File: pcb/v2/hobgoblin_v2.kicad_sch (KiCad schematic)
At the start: 47 parts, among them J1 5V, J2 RC2014EXT1, J3 RC2014EXT2, SW1 RESET, SW2 ROMBNK, SW3 USBUART, U1 74LS32, U10 MC68B50, U2 74LS14, U3 Z80CPU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

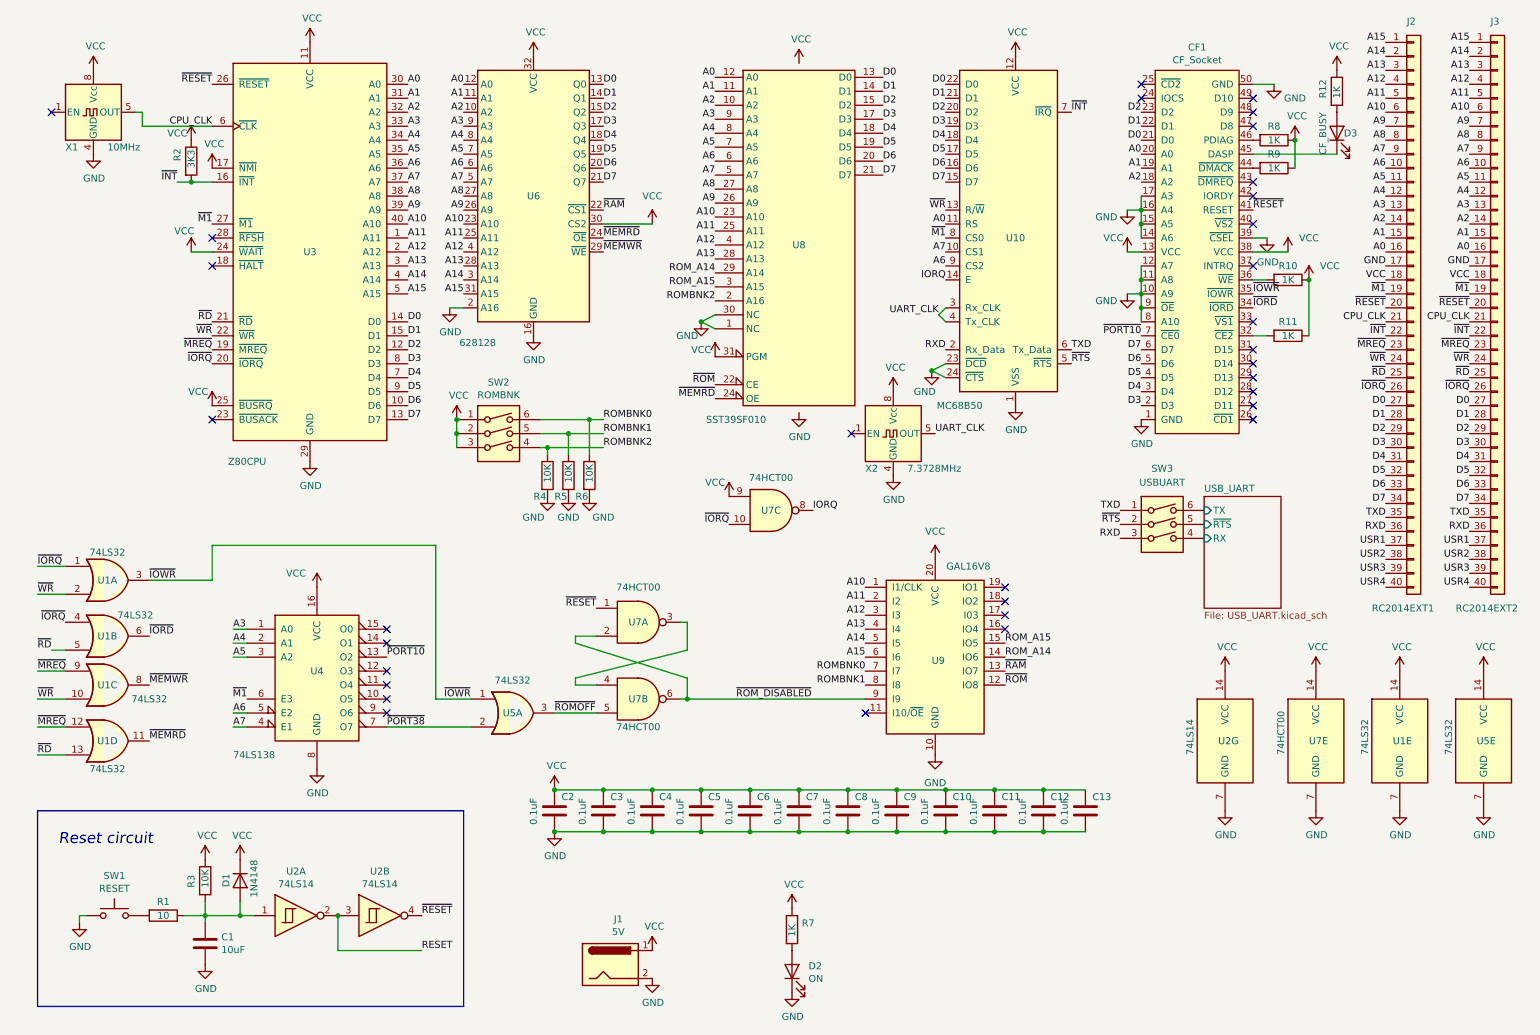
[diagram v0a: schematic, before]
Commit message: Start using GALs in V2
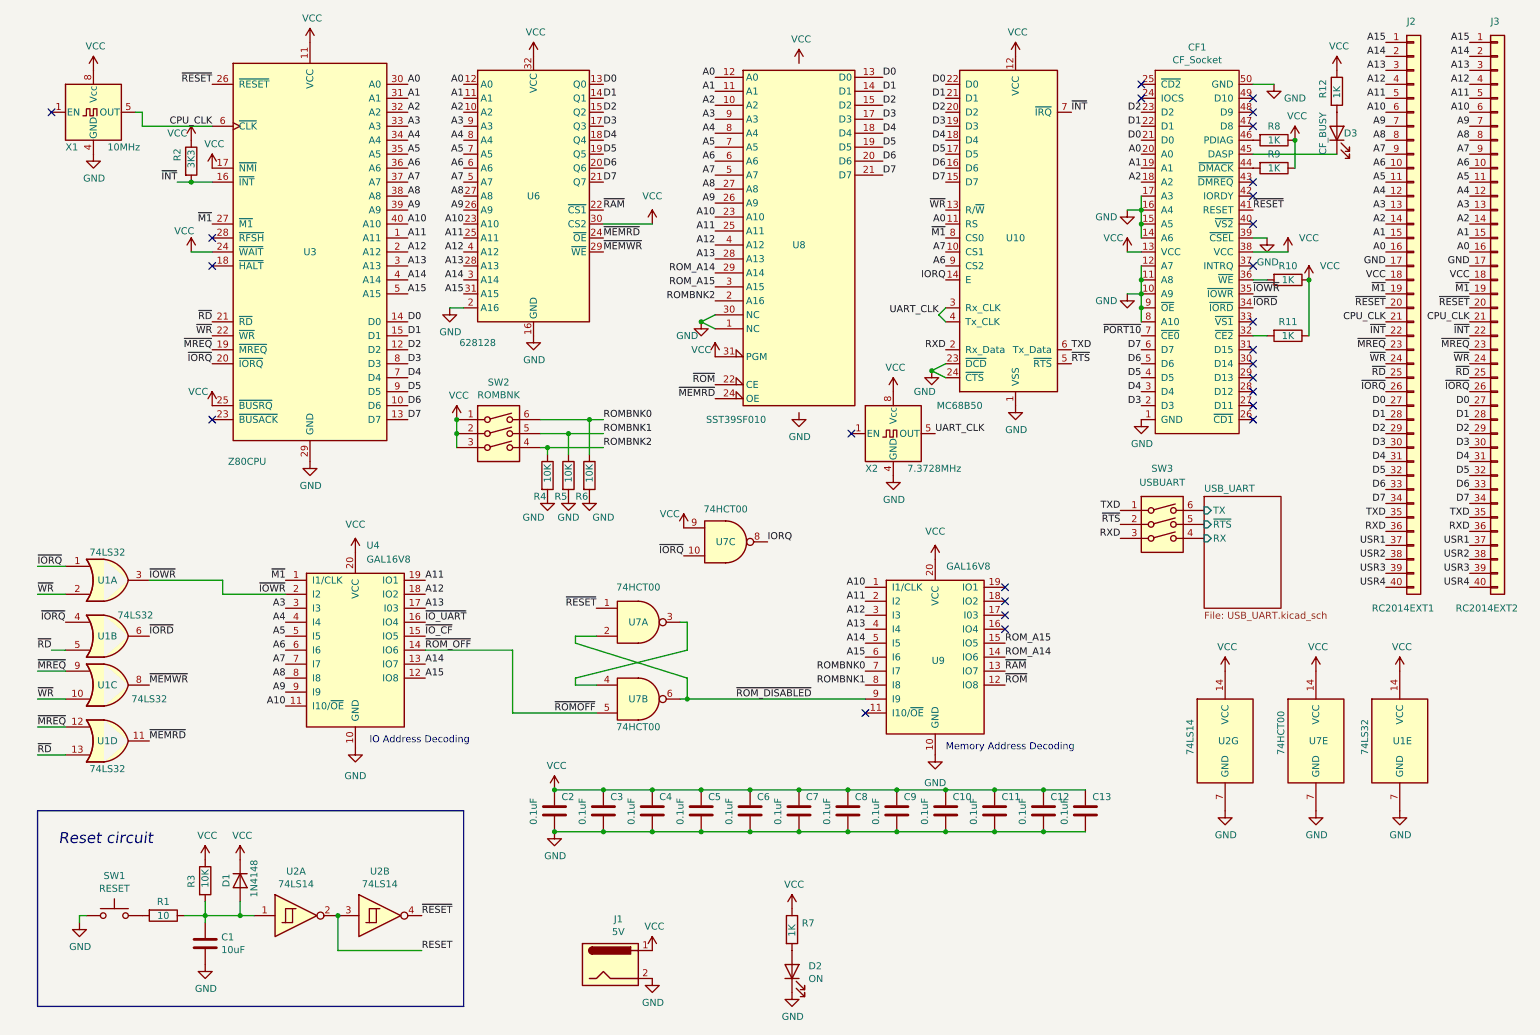
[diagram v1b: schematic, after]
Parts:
- removed U4: 74LS138, Package_DIP:DIP-16_W7.62mm_LongPads, symbol 74xx:74LS138
- removed U5: 74LS32, Package_DIP:DIP-14_W7.62mm_LongPads, symbol 74xx:74LS32
- added U4: GAL16V8, Package_DIP:DIP-20_W7.62mm_Socket_LongPads, symbol Logic_Programmable:GAL16V8
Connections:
- net A10: now also U4.11 (I10/~{OE})
- net A11: now also U4.19 (IO1)
- net A12: now also U4.18 (IO2)
- net A13: now also U4.17 (I03)
- net A14: now also U4.13 (IO7)
- net A15: now also U4.12 (IO8)
- net A3: now also U4.3 (I3)
- net A4: now also U4.4 (I4)
- net A5: now also U4.5 (I5)
- net A6: now also U4.6 (I6)
- net A7: now also U4.7 (I7)
- net A8: now also U4.8 (I8)
- net A9: now also U4.9 (I9)
- net GND: now also U4.10 (GND)
- net VCC: now also U4.20 (VCC)
- net ~{IOWR}: now also U4.2 (I2)
- net ~{M1}: now also U4.1 (I1/CLK)
- net ~{ROMOFF}: now also U4.14 (IO6)
- new net ~{IO_CF}: U4.15 (IO5)
- new net ~{IO_UART}: U4.16 (IO4)
- no-connect marks 32 -> 26
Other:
- note added: "IO Address Decoding"
- note added: "Memory Address Decoding"
- moved on the sheet: U7C

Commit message: Draft component placement
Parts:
- U4: value GAL16V8 -> GAL16V8/IO
- U9: value GAL16V8 -> GAL16V8/MEM
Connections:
- net ~{PORT10} is gone; now on net ~{IO_CF}: CF1.7 (~{CE0})
- net A6: no longer U10.9 (CS2)
- net A7: no longer U10.10 (CS1)
- net ~{IO_UART}: now also U10.9 (CS2)
- net ~{M1}: no longer U10.8 (CS0)
- net ~{ROMOFF} renamed ~{ROM_OFF}
- no-connect marks 26 -> 28
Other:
- moved on the sheet: X2

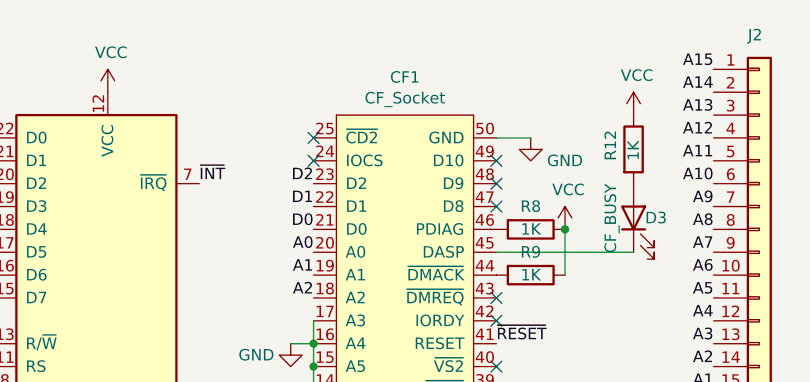
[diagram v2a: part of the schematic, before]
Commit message: CF socket properties
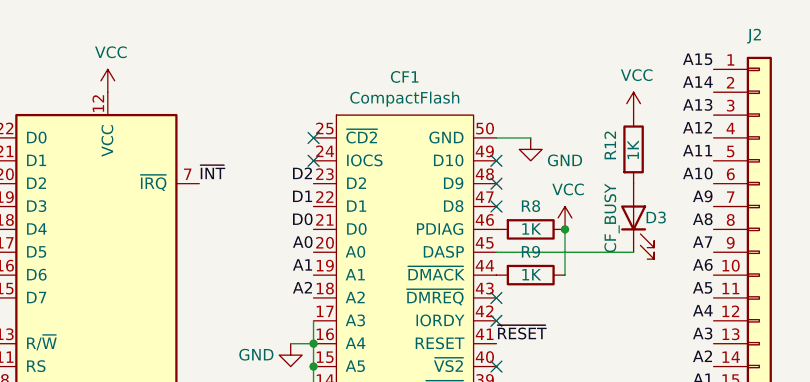
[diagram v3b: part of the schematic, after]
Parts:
- CF1: value CF_Socket -> CompactFlash
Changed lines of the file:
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@@
     (in_bom yes) (on_board yes)
     (property "Reference" "CF1" (id 0) (at 226.06 18.669 0))
-    (property "Value" "CF_Socket" (id 1) (at 226.06 20.9804 0))
+    (property "Value" "CompactFlash" (id 1) (at 226.06 20.9804 0))
     (property "Footprint" "hobgoblin:CF-Card_3M_N7E507516PK20" (id 2) (at 226.06 57.15 0)
       (effects (font (size 1.27 1.27)) hide)
@@
     )
     (path "/00000000-0000-0000-0000-00005fec22e8"
-      (reference "CF1") (unit 1) (value "CF_Socket") (footprint "hobgoblin:CF-Card_3M_N7E507516PK20")
+      (reference "CF1") (unit 1) (value "CompactFlash") (footprint "hobgoblin:CF-Card_3M_N7E507516PK20")
     )
     (path "/00000000-0000-0000-0000-00005f8c4542"

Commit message: PCB layout in progress
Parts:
- removed SW3: USBUART, Button_Switch_THT:SW_DIP_SPSTx03_Slide_6.7x9.18mm_W7.62mm_P2.54mm_LowProfile, symbol Switch:SW_DIP_x03
- added J5: USBUART, Connector_PinHeader_2.54mm:PinHeader_2x03_P2.54mm_Vertical, symbol Connector_Generic:Conn_02x03_Odd_Even
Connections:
- net RXD: now also J5.5 (Pin_5)
- net TXD: now also J5.1 (Pin_1)
- net USB_UART/RX: now also J5.6 (Pin_6)
- net USB_UART/TX: now also J5.2 (Pin_2)
- net USB_UART/~{RTS}: now also J5.4 (Pin_4)
- net ~{RTS}: now also J5.3 (Pin_3)
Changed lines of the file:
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@@
     (effects (font (size 1.27 1.27)) (justify left bottom))
   )
-  (label "TXD" (at 212.09 102.87 180)
+  (label "TXD" (at 214.63 102.87 180)
     (effects (font (size 1.27 1.27)) (justify right bottom))
   )
@@
     (effects (font (size 1.27 1.27)) (justify right bottom))
   )
-  (label "~{RTS}" (at 212.09 105.41 180)
+  (label "~{RTS}" (at 214.63 105.41 180)
     (effects (font (size 1.27 1.27)) (justify right bottom))
   )
@@
     (effects (font (size 1.27 1.27)) (justify right bottom))
   )
-  (label "RXD" (at 212.09 107.95 180)
+  (label "RXD" (at 214.63 107.95 180)
     (effects (font (size 1.27 1.27)) (justify right bottom))
   )
@@
     (pin "1")
   )
-  (symbol (lib_id "power:GND") (at 178.435 147.32 0) (unit 1)
+  (symbol (lib_id "Connector_Generic:Conn_02x03_Odd_Even") (at 219.71 105.41 0) (unit 1)
     (in_bom yes) (on_board yes) (fields_autoplaced)
-    (property "Reference" "#PWR037" (id 0) (at 178.435 153.67 0)
-      (effects (font (size 1.27 1.27)) hide)
-    )
-    (property "Value" "GND" (id 1) (at 178.435 152.4 0))
-    (property "Footprint" "" (id 2) (at 178.435 147.32 0)
-      (effects (font (size 1.27 1.27)) hide)
-    )
-    (property "Datasheet" "" (id 3) (at 178.435 147.32 0)
-      (effects (font (size 1.27 1.27)) hide)
-    )
-    (pin "1")
-  )
-  (symbol (lib_id "Switch:SW_DIP_x03") (at 219.71 107.95 0) (unit 1)
-    (in_bom yes) (on_board yes) (fields_autoplaced)
-    (property "Reference" "SW3" (id 0) (at 219.71 95.25 0))
-    (property "Value" "USBUART" (id 1) (at 219.71 97.79 0))
-    (property "Footprint" "Button_Switch_THT:SW_DIP_SPSTx03_Slide_6.7x9.18mm_W7.62mm_P2.54mm_LowProfile" (id 2) (at 219.71 107.95 0)
-      (effects (font (size 1.27 1.27)) hide)
-    )
-    (property "Datasheet" "~" (id 3) (at 219.71 107.95 0)
+    (property "Reference" "J5" (id 0) (at 220.98 96.52 0))
+    (property "Value" "USBUART" (id 1) (at 220.98 99.06 0))
+    (property "Footprint" "Connector_PinHeader_2.54mm:PinHeader_2x03_P2.54mm_Vertical" (id 2) (at 219.71 105.41 0)
+      (effects (font (size 1.27 1.27)) hide)
+    )
+    (property "Datasheet" "~" (id 3) (at 219.71 105.41 0)
       (effects (font (size 1.27 1.27)) hide)
     )
@@
     (pin "5")
     (pin "6")
+  )
+  (symbol (lib_id "power:GND") (at 178.435 147.32 0) (unit 1)
+    (in_bom yes) (on_board yes) (fields_autoplaced)
+    (property "Reference" "#PWR037" (id 0) (at 178.435 153.67 0)
+      (effects (font (size 1.27 1.27)) hide)
+    )
+    (property "Value" "GND" (id 1) (at 178.435 152.4 0))
+    (property "Footprint" "" (id 2) (at 178.435 147.32 0)
+      (effects (font (size 1.27 1.27)) hide)
+    )
+    (property "Datasheet" "" (id 3) (at 178.435 147.32 0)
+      (effects (font (size 1.27 1.27)) hide)
+    )
+    (pin "1")
   )
   (symbol (lib_id "power:GND") (at 73.025 146.05 0) (unit 1)
@@
       (reference "J4") (unit 1) (value "MINIUSB") (footprint "Connector_USB:USB_Mini-B_Lumberg_2486_01_Horizontal")
     )
+    (path "/8504bada-cd41-46e9-9f33-b89f6fbc6172"
+      (reference "J5") (unit 1) (value "USBUART") (footprint "Connector_PinHeader_2.54mm:PinHeader_2x03_P2.54mm_Vertical")
+    )
     (path "/00000000-0000-0000-0000-00005fcb0453/38651e8c-6527-436e-9fc4-c9859c280385"
       (reference "JP1") (unit 1) (value "USB_VCC") (footprint "Connector_PinSocket_2.54mm:PinSocket_1x02_P2.54mm_Vertical")
@@
       (reference "SW2") (unit 1) (value "ROMBNK") (footprint "Button_Switch_THT:SW_DIP_SPSTx03_Slide_6.7x9.18mm_W7.62mm_P2.54mm_LowProfile")
     )
-    (path "/a4b896b0-a9c1-4c92-b8c2-a20afb00ab8c"
-      (reference "SW3") (unit 1) (value "USBUART") (footprint "Button_Switch_THT:SW_DIP_SPSTx03_Slide_6.7x9.18mm_W7.62mm_P2.54mm_LowProfile")
-    )
     (path "/00000000-0000-0000-0000-00005fb3b054"
